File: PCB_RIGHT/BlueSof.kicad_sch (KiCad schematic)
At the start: 88 parts, among them J1 USB_C_Receptacle_USB2.0, J12 SM02B-SRSS-TB(LF)(SN), Q2 A03407, SW1 SW_PUSH, SW10 SW_PUSH, SW11 SW_PUSH, SW12 SW_PUSH, SW13 SW_PUSH, SW14 SW_PUSH, SW15 SW_PUSH, SW16 SW_PUSH, SW17 SW_PUSH, SW18 SW_PUSH, SW19 SW_PUSH, SW2 SW_PUSH, SW20 SW_PUSH, SW21 SW_PUSH, SW22 SW_PUSH, SW23 SW_PUSH, SW24 SW_PUSH, SW25 Rotary_Encoder_Switch, SW26 SW_PUSH, SW27 SW_PUSH, SW28 SW_PUSH, SW3 SW_PUSH, SW4 SW_PUSH, SW5 SW_PUSH, SW6 SW_PUSH, SW7 SW_PUSH, SW8 SW_PUSH, SW9 SW_PUSH, U1 LN2054Y42AMR, U2 E73-2G4M08S1C, U3 AP2112K-3.3, Y1 32.768kHz

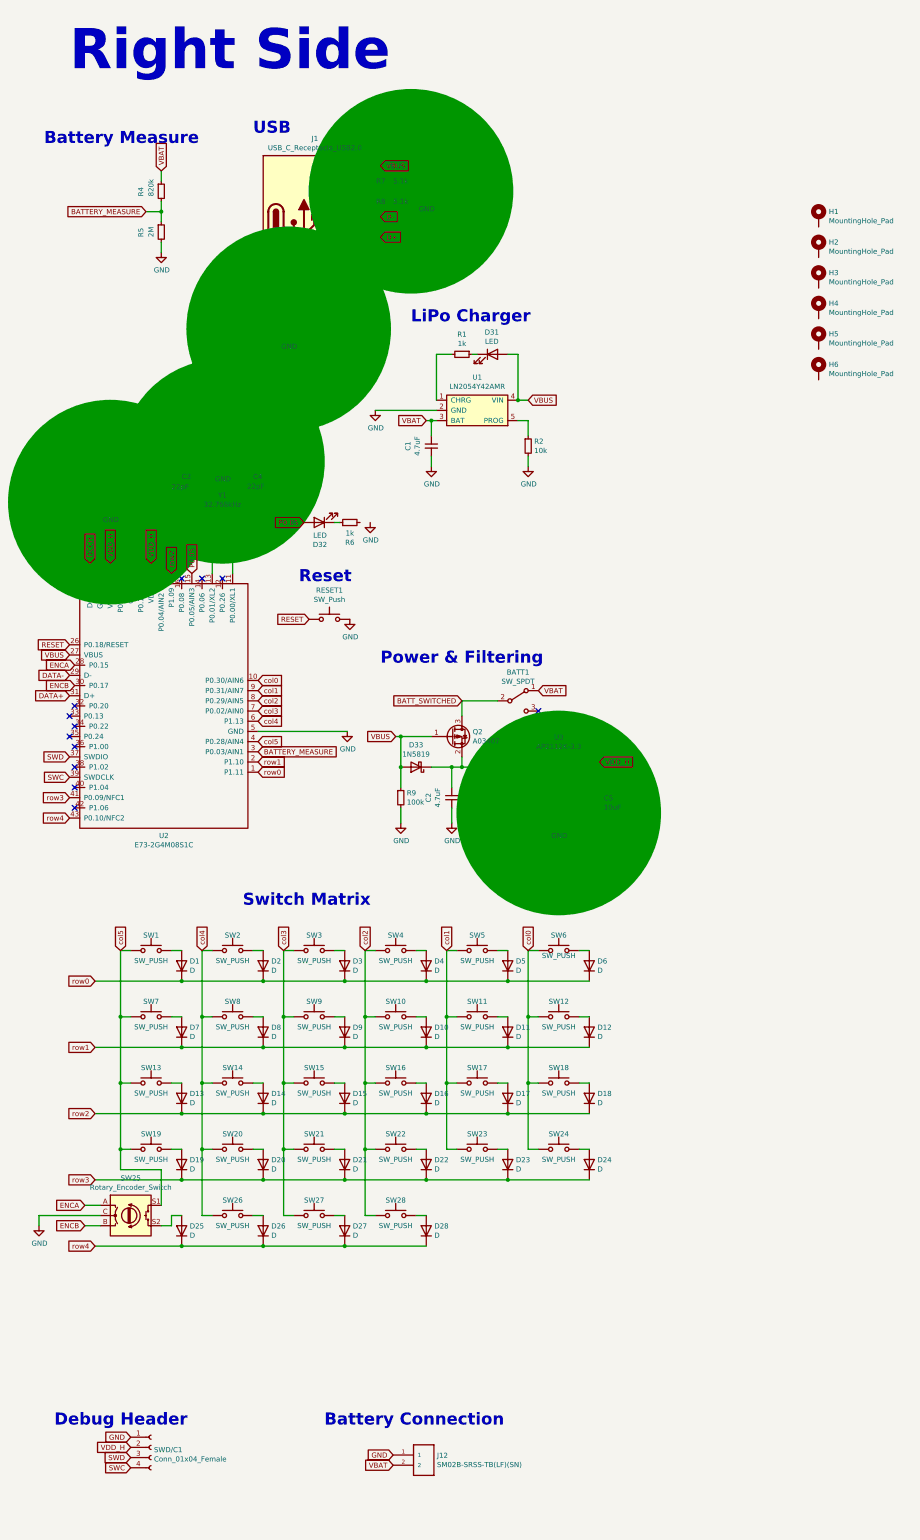
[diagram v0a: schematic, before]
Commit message: ordered left side from jlc
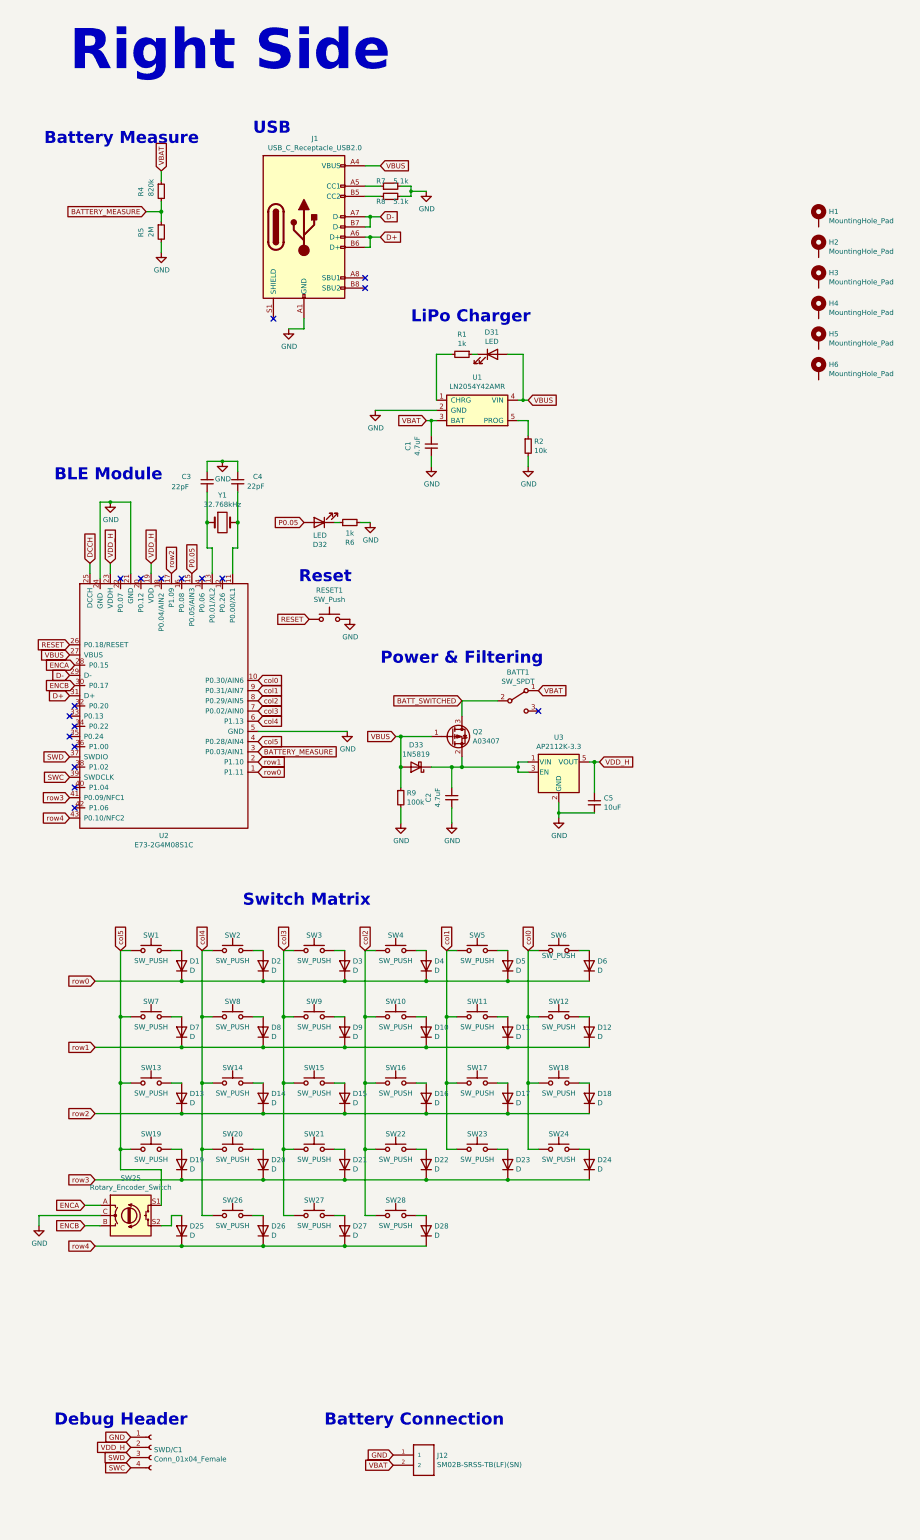
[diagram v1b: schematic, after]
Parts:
- J12: footprint BlueSof:SM02B-SRSS-TB(LF)(SN) -> SM02B-SRSS-TB(LF)(SN); symbol SM02B-SRSS-TB_LF__SN_:SM02B-SRSS-TB(LF)(SN) -> BlueSof:SM02B-SRSS-TB(LF)(SN)
- U1: symbol BlueSof-rescue:LN2054Y42AMR-ELLOW -> BlueSof:LN2054Y42AMR
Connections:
- net DATA+ is gone; now on net D+: U2.31 (D+)
- net DATA- is gone; now on net D-: U2.29 (D-)
- net GND: now also R6.2; no longer J1.S1 (SHIELD)
- no-connect marks 17 -> 18
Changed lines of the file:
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@@
     (rev "R1")
   )
-  (junction (at 325.12 146.05) (diameter 50.9956) (color 0 0 0 0))
+  (junction (at 325.12 146.05) (diameter 0.9144) (color 0 0 0 0))
   (junction (at 327.66 274.32) (diameter 1.016) (color 0 0 0 0))
   (junction (at 327.66 290.83) (diameter 1.016) (color 0 0 0 0))
@@
   (junction (at 347.98 307.34) (diameter 1.016) (color 0 0 0 0))
   (junction (at 349.25 151.13) (diameter 1.016) (color 0 0 0 0))
-  (junction (at 353.06 135.89) (diameter 50.9956) (color 0 0 0 0))
+  (junction (at 353.06 135.89) (diameter 0.9144) (color 0 0 0 0))
   (junction (at 356.87 151.13) (diameter 1.016) (color 0 0 0 0))
   (junction (at 363.22 265.43) (diameter 1.016) (color 0 0 0 0))
@@
   (junction (at 368.3 290.83) (diameter 1.016) (color 0 0 0 0))
   (junction (at 368.3 307.34) (diameter 1.016) (color 0 0 0 0))
-  (junction (at 369.57 102.87) (diameter 51) (color 0 0 0 0))
   (junction (at 383.54 265.43) (diameter 1.016) (color 0 0 0 0))
   (junction (at 383.54 281.94) (diameter 1.016) (color 0 0 0 0))
@@
   (junction (at 397.51 204.47) (diameter 1.016) (color 0 0 0 0))
   (junction (at 397.51 212.09) (diameter 1.016) (color 0 0 0 0))
-  (junction (at 400.05 68.58) (diameter 51) (color 0 0 0 0))
+  (junction (at 400.05 68.58) (diameter 0.9144) (color 0 0 0 0))
   (junction (at 403.86 265.43) (diameter 1.016) (color 0 0 0 0))
   (junction (at 403.86 281.94) (diameter 1.016) (color 0 0 0 0))
   (junction (at 403.86 298.45) (diameter 1.016) (color 0 0 0 0))
   (junction (at 403.86 314.96) (diameter 1.016) (color 0 0 0 0))
-  (junction (at 405.13 125.73) (diameter 1.016) (color 0 0 0 0))
+  (junction (at 405.13 125.73) (diameter 0.9144) (color 0 0 0 0))
   (junction (at 408.94 274.32) (diameter 1.016) (color 0 0 0 0))
   (junction (at 408.94 290.83) (diameter 1.016) (color 0 0 0 0))
@@
   (junction (at 424.18 298.45) (diameter 1.016) (color 0 0 0 0))
   (junction (at 424.18 314.96) (diameter 1.016) (color 0 0 0 0))
-  (junction (at 426.72 120.65) (diameter 1.016) (color 0 0 0 0))
   (junction (at 426.72 212.09) (diameter 1.016) (color 0 0 0 0))
+  (junction (at 427.99 120.65) (diameter 0.9144) (color 0 0 0 0))
   (junction (at 429.26 274.32) (diameter 1.016) (color 0 0 0 0))
   (junction (at 429.26 290.83) (diameter 1.016) (color 0 0 0 0))
-  (junction (at 436.88 223.52) (diameter 50.9956) (color 0 0 0 0))
+  (junction (at 436.88 223.52) (diameter 0.9144) (color 0 0 0 0))
   (junction (at 445.77 210.82) (diameter 1.016) (color 0 0 0 0))
   (no_connect (at 314.96 199.39))
@@
   (no_connect (at 347.98 165.1))
   (no_connect (at 353.06 165.1))
+  (no_connect (at 365.76 100.33))
   (no_connect (at 388.62 90.17))
   (no_connect (at 388.62 92.71))
@@
     (stroke (width 0) (type solid) (color 0 0 0 0))
   )
-  (wire (pts (xy 365.76 100.33) (xy 365.76 102.87))
-    (stroke (width 0) (type solid) (color 0 0 0 0))
-  )
-  (wire (pts (xy 365.76 102.87) (xy 369.57 102.87))
-    (stroke (width 0) (type solid) (color 0 0 0 0))
-  )
   (wire (pts (xy 368.3 257.81) (xy 368.3 274.32))
     (stroke (width 0) (type solid) (color 0 0 0 0))
@@
     (stroke (width 0) (type solid) (color 0 0 0 0))
   )
+  (wire (pts (xy 387.35 151.13) (xy 389.89 151.13))
+    (stroke (width 0) (type solid) (color 0 0 0 0))
+  )
   (wire (pts (xy 388.62 74.93) (xy 389.89 74.93))
     (stroke (width 0) (type solid) (color 0 0 0 0))
@@
     (stroke (width 0) (type solid) (color 0 0 0 0))
   )
+  (wire (pts (xy 405.13 125.73) (xy 406.4 125.73))
+    (stroke (width 0) (type solid) (color 0 0 0 0))
+  )
   (wire (pts (xy 405.13 134.62) (xy 405.13 137.16))
     (stroke (width 0) (type solid) (color 0 0 0 0))
@@
     (stroke (width 0) (type solid) (color 0 0 0 0))
   )
-  (wire (pts (xy 406.4 125.73) (xy 405.13 125.73))
-    (stroke (width 0) (type solid) (color 0 0 0 0))
-  )
   (wire (pts (xy 408.94 257.81) (xy 408.94 274.32))
     (stroke (width 0) (type solid) (color 0 0 0 0))
@@
     (stroke (width 0) (type solid) (color 0 0 0 0))
   )
+  (wire (pts (xy 424.18 109.22) (xy 427.99 109.22))
+    (stroke (width 0) (type solid) (color 0 0 0 0))
+  )
   (wire (pts (xy 424.18 265.43) (xy 403.86 265.43))
     (stroke (width 0) (type solid) (color 0 0 0 0))
@@
     (stroke (width 0) (type solid) (color 0 0 0 0))
   )
-  (wire (pts (xy 426.72 109.22) (xy 424.18 109.22))
-    (stroke (width 0) (type solid) (color 0 0 0 0))
-  )
-  (wire (pts (xy 426.72 120.65) (xy 426.72 109.22))
+  (wire (pts (xy 426.72 120.65) (xy 427.99 120.65))
     (stroke (width 0) (type solid) (color 0 0 0 0))
   )
@@
     (stroke (width 0) (type solid) (color 0 0 0 0))
   )
-  (wire (pts (xy 429.26 120.65) (xy 426.72 120.65))
+  (wire (pts (xy 427.99 109.22) (xy 427.99 120.65))
+    (stroke (width 0) (type solid) (color 0 0 0 0))
+  )
+  (wire (pts (xy 427.99 120.65) (xy 429.26 120.65))
     (stroke (width 0) (type solid) (color 0 0 0 0))
   )
@@
     (effects (font (size 1.27 1.27)) (justify right))
   )
-  (global_label "DATA-" (shape input) (at 314.96 189.23 180)    (property "Intersheet References" "${INTERSHEET_REFS}" (id 0) (at 95.25 -6.35 0)
-      (effects (font (size 1.27 1.27)) hide)
-    )
-    (effects (font (size 1.27 1.27)) (justify right))
-  )
-  (global_label "DATA+" (shape input) (at 314.96 194.31 180)    (property "Intersheet References" "${INTERSHEET_REFS}" (id 0) (at 95.25 -6.35 0)
-      (effects (font (size 1.27 1.27)) hide)
+  (global_label "D-" (shape input) (at 314.96 189.23 180)    (property "Intersheet References" "${INTERSHEET_REFS}" (id 0) (at 308.1805 189.1506 0)
+      (effects (font (size 1.27 1.27)) (justify right) hide)
+    )
+    (effects (font (size 1.27 1.27)) (justify right))
+  )
+  (global_label "D+" (shape input) (at 314.96 194.31 180)    (property "Intersheet References" "${INTERSHEET_REFS}" (id 0) (at 308.1805 194.2306 0)
+      (effects (font (size 1.27 1.27)) (justify right) hide)
     )
     (effects (font (size 1.27 1.27)) (justify right))
@@
     )
   )
-  (symbol (lib_id "SM02B-SRSS-TB_LF__SN_:SM02B-SRSS-TB(LF)(SN)") (at 395.605 388.62 0) (unit 1)
+  (symbol (lib_id "BlueSof:SM02B-SRSS-TB(LF)(SN)") (at 395.605 388.62 0) (unit 1)
     (in_bom yes) (on_board yes)
     (property "Reference" "J12" (id 0) (at 406.5271 383.6606 0)
@@
       (effects (font (size 1.27 1.27)) (justify left))
     )
-    (property "Footprint" "BlueSof:SM02B-SRSS-TB(LF)(SN)" (id 2) (at 395.605 388.62 0)
+    (property "Footprint" "SM02B-SRSS-TB(LF)(SN)" (id 2) (at 395.605 388.62 0)
       (effects (font (size 1.27 1.27)) (justify left bottom) hide)
     )
@@
     )
   )
-  (symbol (lib_id "BlueSof-rescue:LN2054Y42AMR-ELLOW") (at 416.56 123.19 0) (unit 1)
+  (symbol (lib_id "BlueSof:LN2054Y42AMR") (at 416.56 123.19 0) (unit 1)
     (in_bom yes) (on_board yes)
     (property "Reference" "U1" (id 0) (at 416.56 114.935 0))
@@
     )
     (path "/854d8cf3-8c16-4b20-a5e1-a1229cd64724"
-      (reference "J12") (unit 1) (value "SM02B-SRSS-TB(LF)(SN)") (footprint "BlueSof:SM02B-SRSS-TB(LF)(SN)")
+      (reference "J12") (unit 1) (value "SM02B-SRSS-TB(LF)(SN)") (footprint "SM02B-SRSS-TB(LF)(SN)")
     )
     (path "/00000000-0000-0000-0000-00005fd315d0"

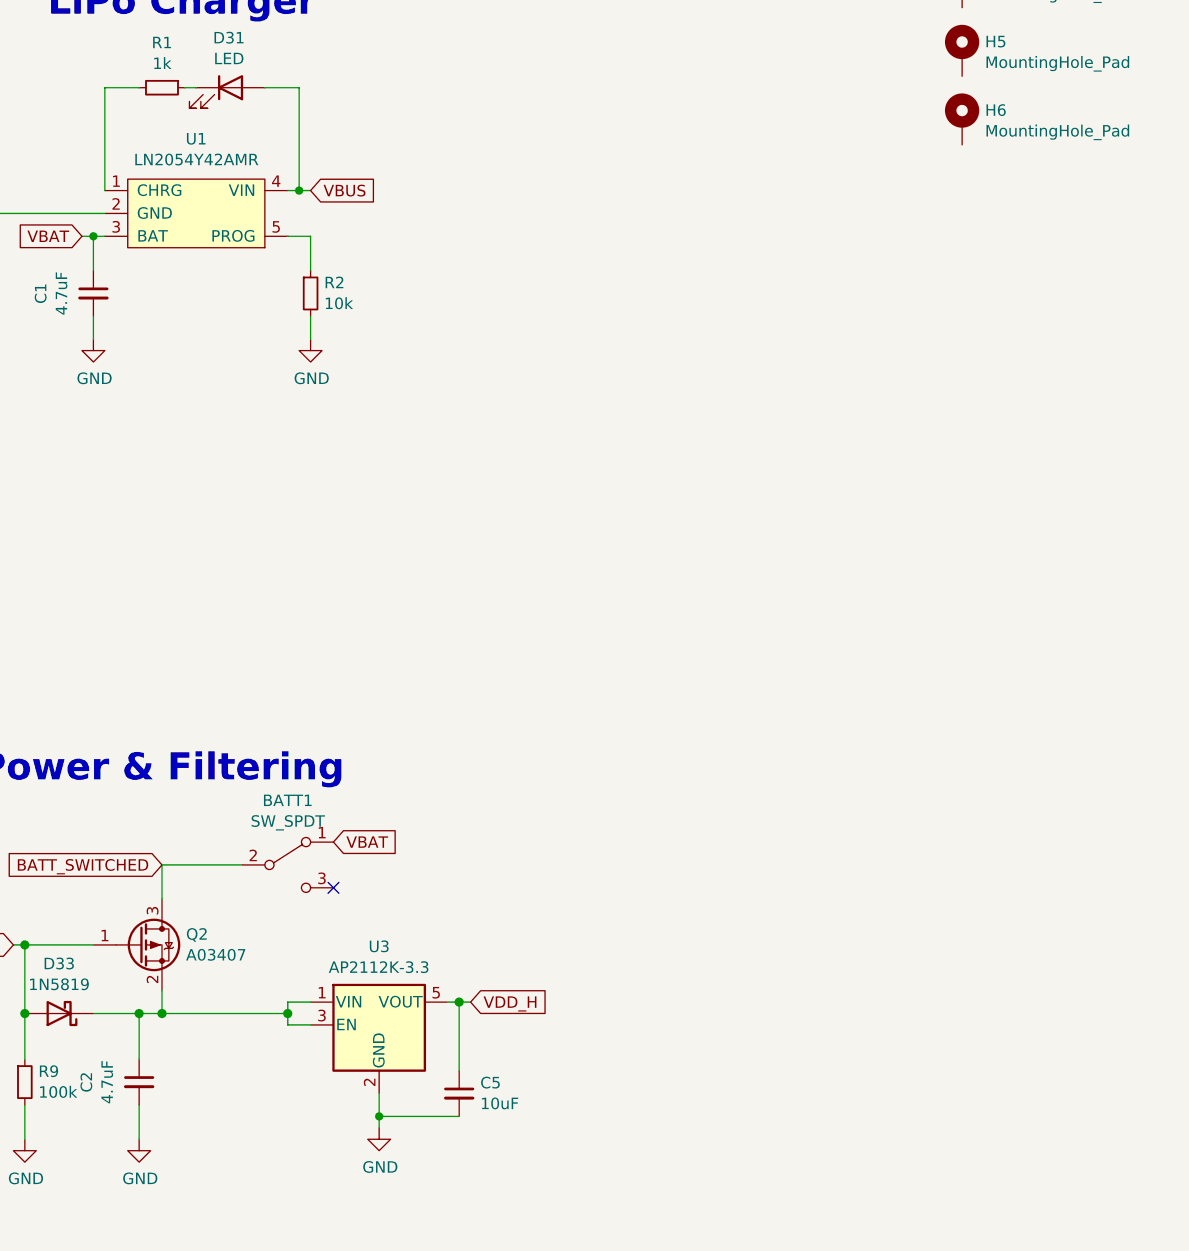
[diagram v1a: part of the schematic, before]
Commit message: minor updates for SMD assembly
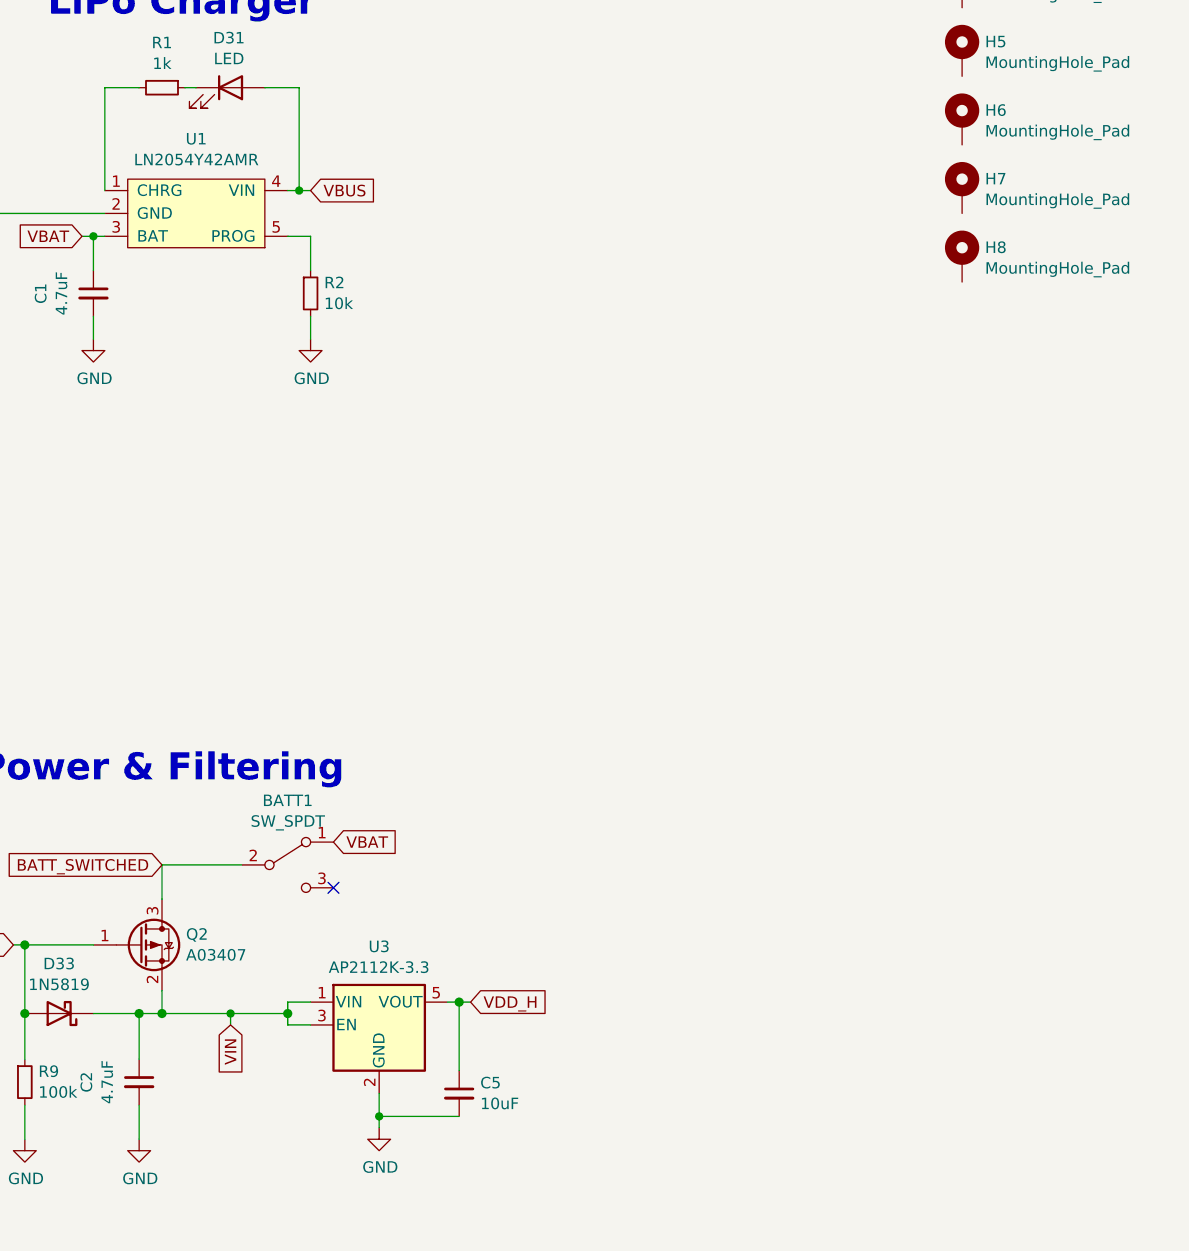
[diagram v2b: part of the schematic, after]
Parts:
- added H7, H8: MountingHole_Pad, MountingHole:MountingHole_4.3mm_M4, symbol Mechanical:MountingHole_Pad
- BATT1: LCSC_PN (none) -> C431540
- C1, C2: footprint Capacitor_SMD:C_0603_1608Metric_Pad1.08x0.95mm_HandSolder -> Capacitor_SMD:C_0603_1608Metric; LCSC_PN (none) -> C19666; PRICE (none) -> 100k
- C3, C4: footprint Capacitor_SMD:C_0603_1608Metric_Pad1.08x0.95mm_HandSolder -> Capacitor_SMD:C_0603_1608Metric; LCSC_PN (none) -> C1653; PRICE (none) -> 100k
- C5: footprint Capacitor_SMD:C_0603_1608Metric_Pad1.08x0.95mm_HandSolder -> Capacitor_SMD:C_0603_1608Metric; LCSC_PN (none) -> C326057; PRICE (none) -> 100k
- D1, D10, D11, D12, D13, D14, D15, D16, D17, D18, D19, D2, D20, D21, D22, D23, D24, D25, D26, D27, D28, D3, D4, D5, D6, D7, D8, D9: LCSC_PN (none) -> C402213; PRICE (none) -> 100k
- D31, D32: footprint LED_SMD:LED_0603_1608Metric_Pad1.05x0.95mm_HandSolder -> LED_SMD:LED_0603_1608Metric; PACKAGE (none) -> 0603; PRICE (none) -> 100k
- D33: LCSC_PN (none) -> C489147; PACKAGE (none) -> SOD-123
- J1: LCSC_PN (none) -> C168688
- J12: footprint SM02B-SRSS-TB(LF)(SN) -> BlueSof:SM02B-SRSS-TB(LF)(SN); LCSC_PN (none) -> C160402
- Q2: LCSC_PN (none) -> C351408; PACKAGE (none) -> SOT-23
- R1, R6: footprint Resistor_SMD:R_0603_1608Metric_Pad0.98x0.95mm_HandSolder -> Resistor_SMD:R_0603_1608Metric; LCSC_PN (none) -> C22548; PRICE (none) -> 5.1k
- R2: footprint Resistor_SMD:R_0603_1608Metric_Pad0.98x0.95mm_HandSolder -> Resistor_SMD:R_0603_1608Metric; LCSC_PN (none) -> C98220; PRICE (none) -> 100k
- R4: footprint Resistor_SMD:R_0603_1608Metric_Pad0.98x0.95mm_HandSolder -> Resistor_SMD:R_0603_1608Metric; LCSC_PN (none) -> C23252; PRICE (none) -> 100k
- R5: footprint Resistor_SMD:R_0603_1608Metric_Pad0.98x0.95mm_HandSolder -> Resistor_SMD:R_0603_1608Metric; LCSC_PN (none) -> C177282; PRICE (none) -> 100k
- R7, R8: footprint Resistor_SMD:R_0603_1608Metric_Pad0.98x0.95mm_HandSolder -> Resistor_SMD:R_0603_1608Metric; LCSC_PN (none) -> C105580; PRICE (none) -> 100k
- R9: footprint Resistor_SMD:R_0603_1608Metric_Pad0.98x0.95mm_HandSolder -> Resistor_SMD:R_0603_1608Metric; LCSC_PN (none) -> C14675; PACKAGE (none) -> 0603
- RESET1: LCSC_PN (none) -> C231329
- U1: LCSC_PN (none) -> C141406; PACKAGE (none) -> SOT-23-5
- U2: LCSC_PN (none) -> C356849
- U3: LCSC_PN (none) -> C51118; PACKAGE (none) -> SOT-23-5
- Y1: LCSC_PN (none) -> C93230; PACKAGE (none) -> 1.6x1.0
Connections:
- net VIN: now reaches C2.1, D33.1 (K), Q2.2 (S), U3.1 (VIN), U3.3 (EN)
